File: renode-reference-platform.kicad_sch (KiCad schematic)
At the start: 28 parts

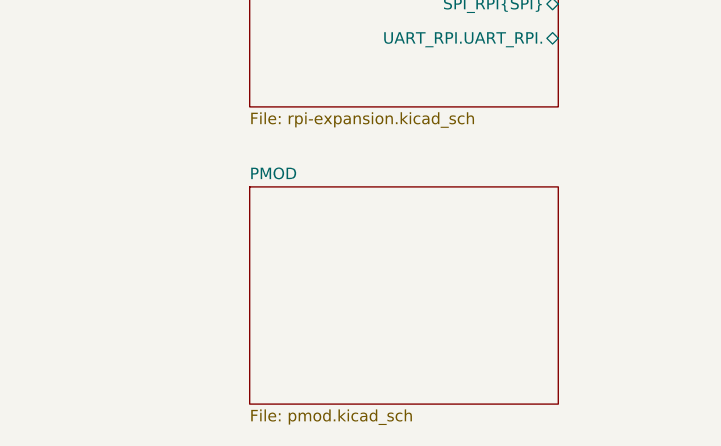
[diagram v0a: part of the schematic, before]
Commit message: [#94862] Add PMOD interfaces
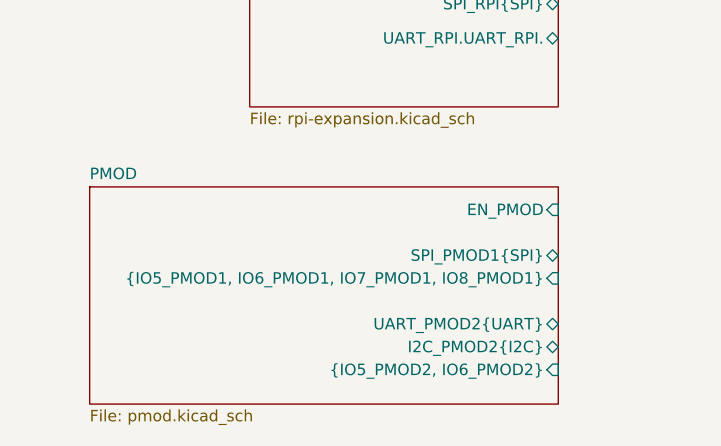
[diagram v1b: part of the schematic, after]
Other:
- sheet PMOD ports: added EN_PMOD, I2C_PMOD2{I2C}, SPI_PMOD1{SPI}, UART_PMOD2{UART}, {IO5_PMOD1, IO6_PMOD1, IO7_PMOD1, IO8_PMOD1}, {IO5_PMOD2, IO6_PMOD2}; removed none
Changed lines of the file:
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@@
 	)
 	(sheet
-		(at 64.77 217.17)
-		(size 34.29 24.13)
+		(at 46.99 217.17)
+		(size 52.07 24.13)
 		(exclude_from_sim no)
 		(in_bom yes)
@@
 		)
 		(property "Sheetname" "PMOD"
-			(at 64.77 216.4584 0)
+			(at 46.99 216.4584 0)
 			(effects
 				(font
@@
 		)
 		(property "Sheetfile" "pmod.kicad_sch"
-			(at 64.77 241.8846 0)
+			(at 46.99 241.8846 0)
 			(effects
 				(font
@@
 			)
 		)
+		(pin "EN_PMOD" input
+			(at 99.06 219.71 0)
+			(effects
+				(font
+					(size 1.27 1.27)
+				)
+				(justify right)
+			)
+		)
+		(pin "I2C_PMOD2{I2C}" bidirectional
+			(at 99.06 234.95 0)
+			(effects
+				(font
+					(size 1.27 1.27)
+				)
+				(justify right)
+			)
+		)
+		(pin "SPI_PMOD1{SPI}" bidirectional
+			(at 99.06 224.79 0)
+			(effects
+				(font
+					(size 1.27 1.27)
+				)
+				(justify right)
+			)
+		)
+		(pin "UART_PMOD2{UART}" bidirectional
+			(at 99.06 232.41 0)
+			(effects
+				(font
+					(size 1.27 1.27)
+				)
+				(justify right)
+			)
+		)
+		(pin "{IO5_PMOD1, IO6_PMOD1, IO7_PMOD1, IO8_PMOD1}" input
+			(at 99.06 227.33 0)
+			(effects
+				(font
+					(size 1.27 1.27)
+				)
+				(justify right)
+			)
+		)
+		(pin "{IO5_PMOD2, IO6_PMOD2}" input
+			(at 99.06 237.49 0)
+			(effects
+				(font
+					(size 1.27 1.27)
+				)
+				(justify right)
+			)
+		)

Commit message: [#94911] Add USB DRP
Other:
- sheet USB-C ports: added I2C_USB{I2C}, USB_GPIO_OUT1, USB_GPIO_OUT2, USB_GPIO_~{INT}; removed none
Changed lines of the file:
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@@
 		)
 		(pin "USB{USB}" bidirectional
+			(at 99.06 123.19 0)
+			(effects
+				(font
+					(size 1.27 1.27)
+				)
+				(justify right)
+			)
+		)
+		(pin "I2C_USB{I2C}" bidirectional
+			(at 99.06 125.73 0)
+			(effects
+				(font
+					(size 1.27 1.27)
+				)
+				(justify right)
+			)
+		)
+		(pin "USB_GPIO_OUT1" input
 			(at 99.06 132.08 0)
 			(effects
 				(font
+					(size 1.27 1.27)
+				)
+				(justify right)
+			)
+		)
+		(pin "USB_GPIO_OUT2" input
+			(at 99.06 134.62 0)
+			(effects
+				(font
+					(size 1.27 1.27)
+				)
+				(justify right)
+			)
+		)
+		(pin "USB_GPIO_~{INT}" input
+			(at 99.06 129.54 0)
+			(effects
+				(font

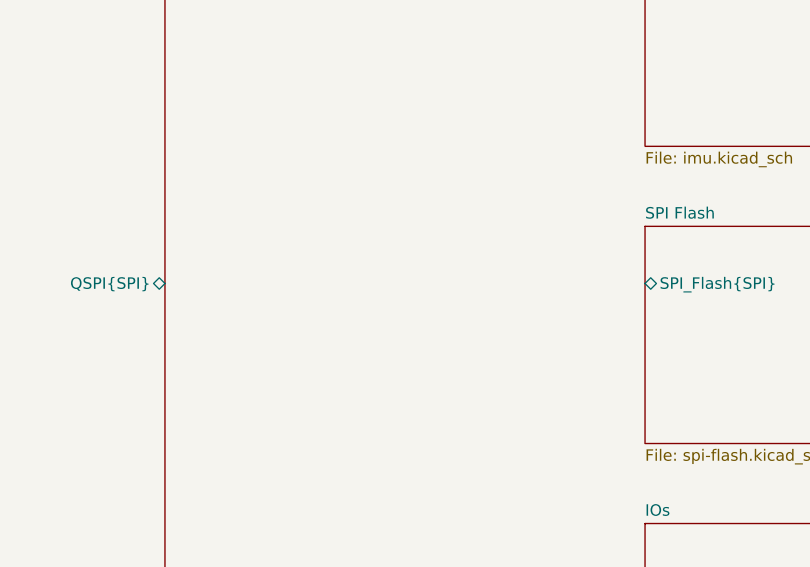
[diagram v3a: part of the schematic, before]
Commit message: [#94972] Reconnect QSPI to MCU
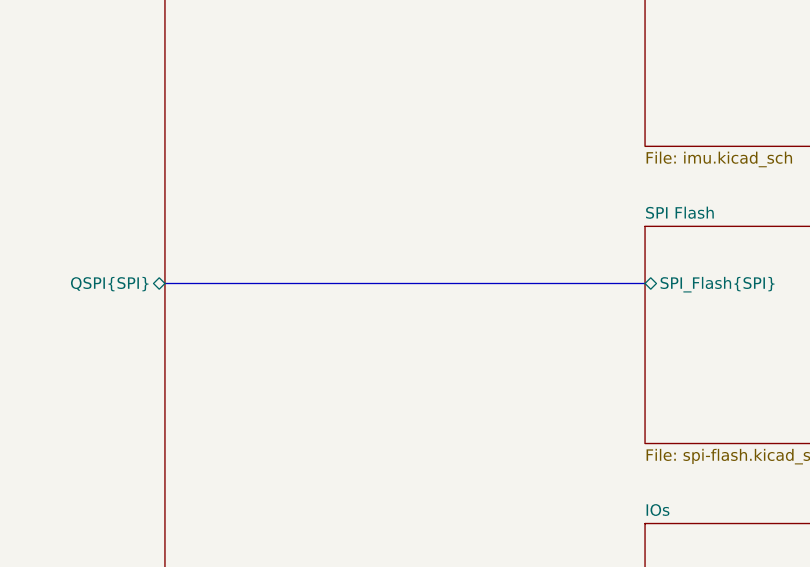
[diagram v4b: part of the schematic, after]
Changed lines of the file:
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@@
+		)
+	)
+	(bus
+		(pts
+			(xy 198.12 157.48) (xy 251.46 157.48)
+		)
+		(stroke
+			(width 0)
+			(type default)
 		)
 	)

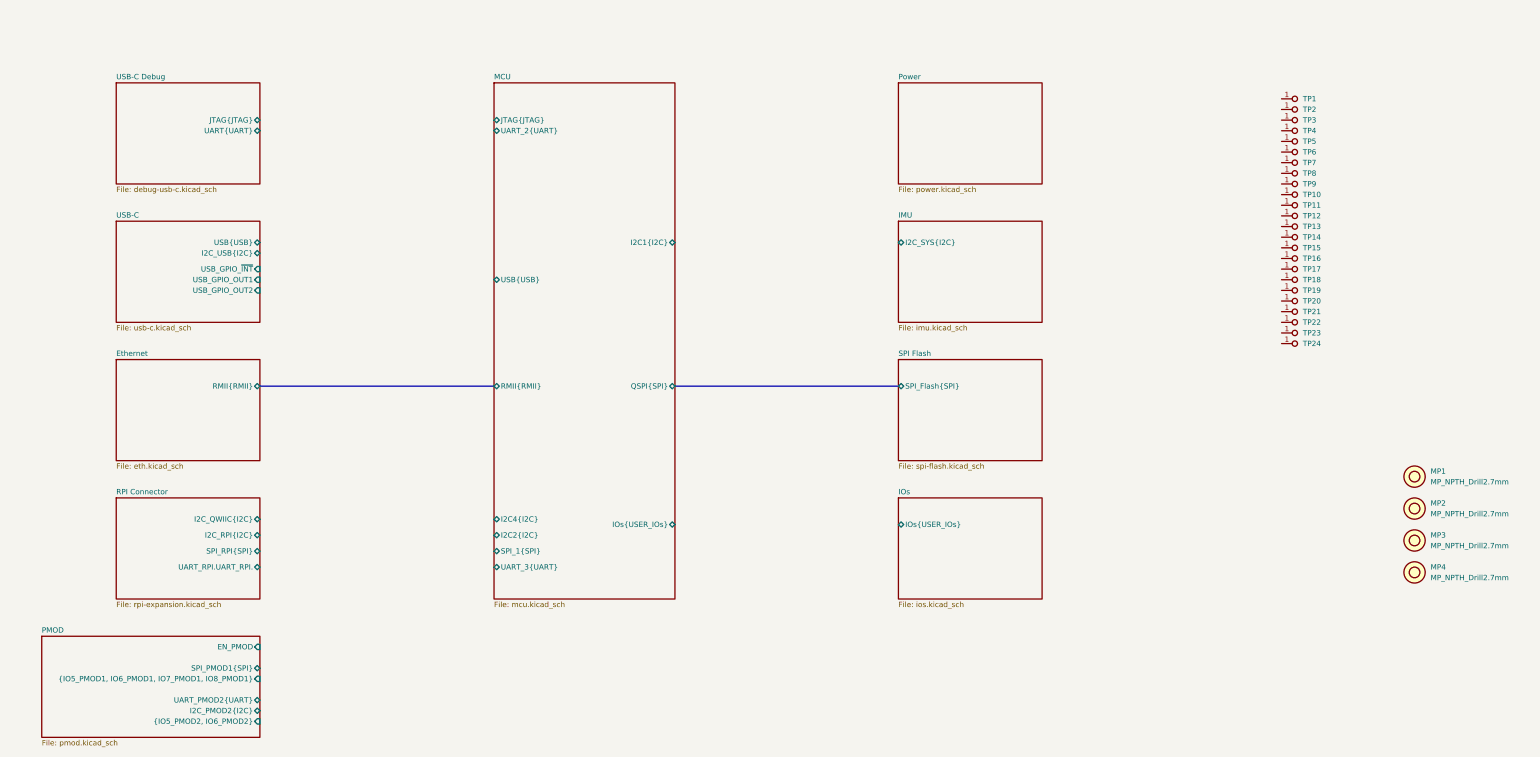
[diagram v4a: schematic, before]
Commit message: [#95036] Rename PMOD signals
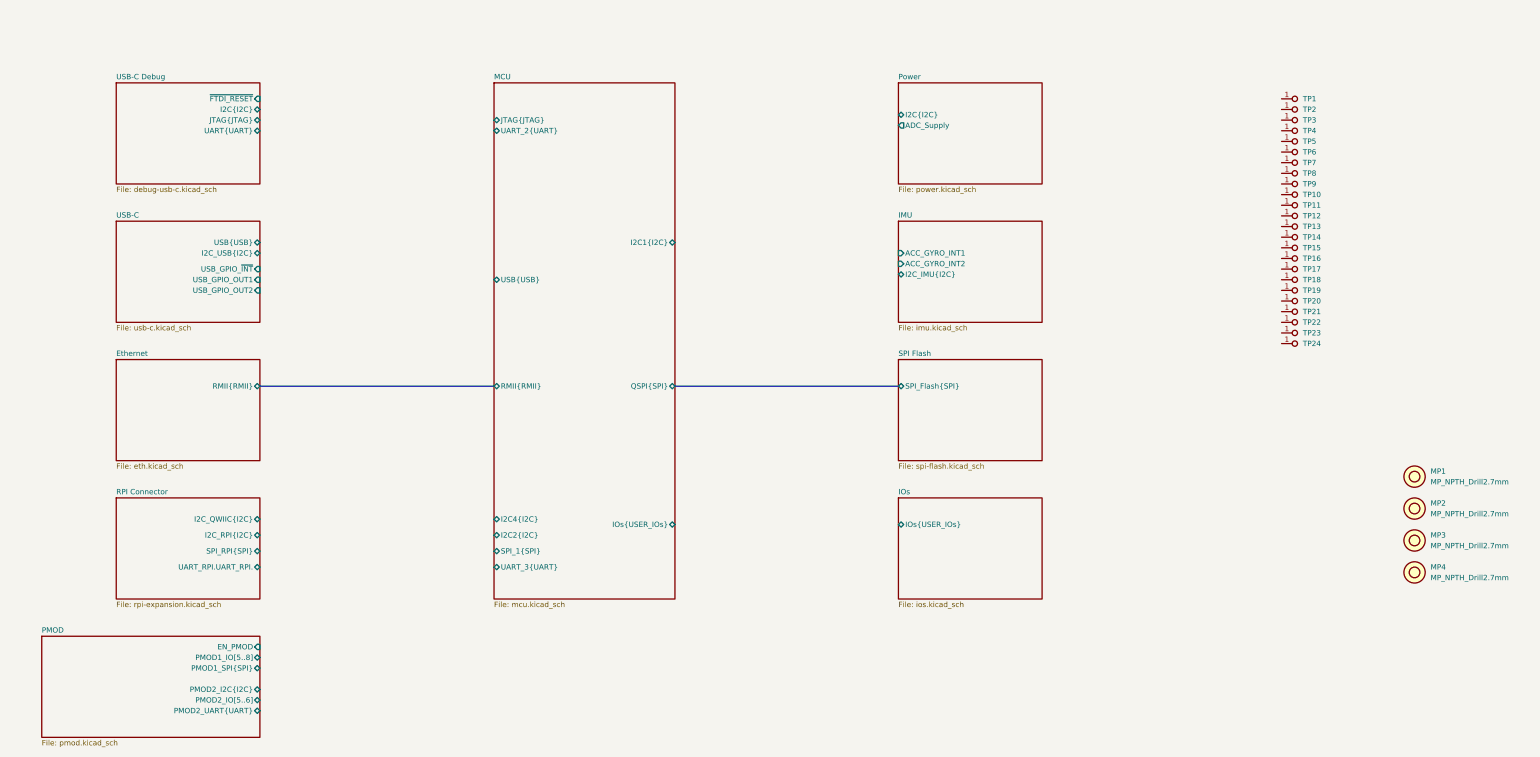
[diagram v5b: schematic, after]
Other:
- sheet IMU ports: added ACC_GYRO_INT1, ACC_GYRO_INT2, I2C_IMU{I2C}; removed I2C_SYS{I2C}
- sheet PMOD ports: added PMOD1_IO[5..8], PMOD1_SPI{SPI}, PMOD2_I2C{I2C}, PMOD2_IO[5..6], PMOD2_UART{UART}; removed I2C_PMOD2{I2C}, SPI_PMOD1{SPI}, UART_PMOD2{UART}, {IO5_PMOD1, IO6_PMOD1, IO7_PMOD1, IO8_PMOD1}, {IO5_PMOD2, IO6_PMOD2}
- sheet Power ports: added ADC_Supply, I2C{I2C}; removed none
- sheet USB-C Debug ports: added I2C{I2C}, ~{FTDI_RESET}; removed none
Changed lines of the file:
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@@
 			)
 		)
-		(pin "I2C_SYS{I2C}" bidirectional
-			(at 251.46 123.19 180)
+		(pin "ACC_GYRO_INT1" input
+			(at 251.46 125.73 180)
+			(effects
+				(font
+					(size 1.27 1.27)
+				)
+				(justify left)
+			)
+		)
+		(pin "ACC_GYRO_INT2" input
+			(at 251.46 128.27 180)
+			(effects
+				(font
+					(size 1.27 1.27)
+				)
+				(justify left)
+			)
+		)
+		(pin "I2C_IMU{I2C}" bidirectional
+			(at 251.46 130.81 180)
 			(effects
 				(font
@@
 			)
 		)
+		(pin "ADC_Supply" output
+			(at 251.46 95.25 180)
+			(effects
+				(font
+					(size 1.27 1.27)
+				)
+				(justify left)
+			)
+		)
+		(pin "I2C{I2C}" bidirectional
+			(at 251.46 92.71 180)
+			(effects
+				(font
+					(size 1.27 1.27)
+				)
+				(justify left)
+			)
+		)
 		(instances
 			(project "renode-reference-platform"
@@
 			)
 		)
-		(pin "I2C_PMOD2{I2C}" bidirectional
+		(pin "PMOD1_IO[5..8]" bidirectional
+			(at 99.06 222.25 0)
+			(effects
+				(font
+					(size 1.27 1.27)
+				)
+				(justify right)
+			)
+		)
+		(pin "PMOD1_SPI{SPI}" bidirectional
+			(at 99.06 224.79 0)
+			(effects
+				(font
+					(size 1.27 1.27)
+				)
+				(justify right)
+			)
+		)
+		(pin "PMOD2_I2C{I2C}" bidirectional
+			(at 99.06 229.87 0)
+			(effects
+				(font
+					(size 1.27 1.27)
+				)
+				(justify right)
+			)
+		)
+		(pin "PMOD2_IO[5..6]" bidirectional
+			(at 99.06 232.41 0)
+			(effects
+				(font
+					(size 1.27 1.27)
+				)
+				(justify right)
+			)
+		)
+		(pin "PMOD2_UART{UART}" bidirectional
 			(at 99.06 234.95 0)
-			(effects
-				(font
-					(size 1.27 1.27)
-				)
-				(justify right)
-			)
-		)
-		(pin "SPI_PMOD1{SPI}" bidirectional
-			(at 99.06 224.79 0)
-			(effects
-				(font
-					(size 1.27 1.27)
-				)
-				(justify right)
-			)
-		)
-		(pin "UART_PMOD2{UART}" bidirectional
-			(at 99.06 232.41 0)
-			(effects
-				(font
-					(size 1.27 1.27)
-				)
-				(justify right)
-			)
-		)
-		(pin "{IO5_PMOD1, IO6_PMOD1, IO7_PMOD1, IO8_PMOD1}" input
-			(at 99.06 227.33 0)
-			(effects
-				(font
-					(size 1.27 1.27)
-				)
-				(justify right)
-			)
-		)
-		(pin "{IO5_PMOD2, IO6_PMOD2}" input
-			(at 99.06 237.49 0)
 			(effects
 				(font
@@
 			(effects
 				(font
+					(size 1.27 1.27)
+				)
+				(justify right)
+			)
+		)
+		(pin "I2C{I2C}" bidirectional
+			(at 99.06 91.44 0)
+			(effects
+				(font
+					(size 1.27 1.27)
+				)
+				(justify right)
+			)
+		)
+		(pin "~{FTDI_RESET}" input
+			(at 99.06 88.9 0)
+			(effects
+				(font

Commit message: [#95036] Reconnect power flags, add GPIOs to RPI connector
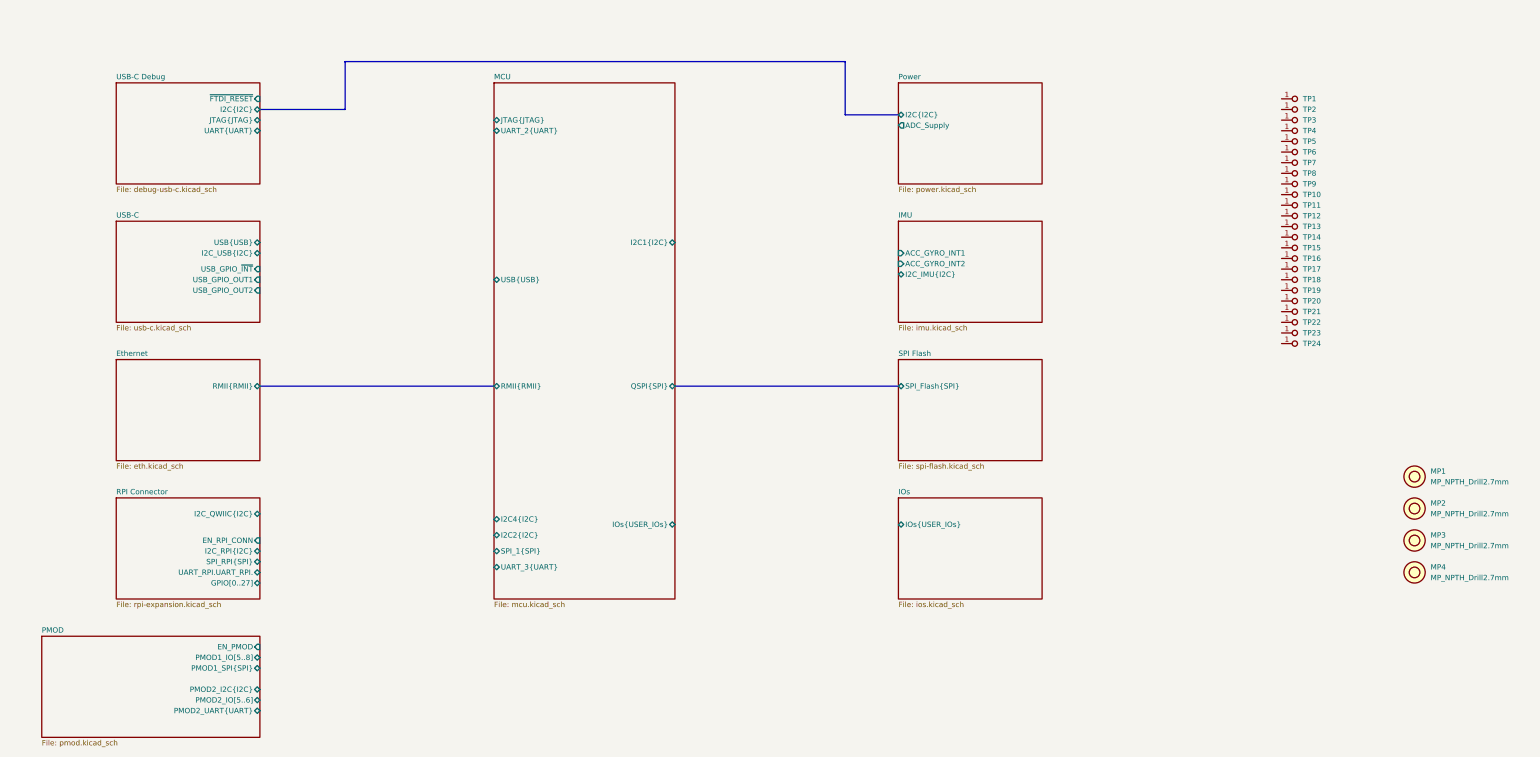
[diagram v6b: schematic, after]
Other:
- sheet RPI Connector ports: added EN_RPI_CONN, GPIO[0..27]; removed none
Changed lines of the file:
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@@
 	(bus
 		(pts
+			(xy 119.38 91.44) (xy 119.38 80.01)
+		)
+		(stroke
+			(width 0)
+			(type default)
+		)
+	)
+	(bus
+		(pts
+			(xy 99.06 91.44) (xy 119.38 91.44)
+		)
+		(stroke
+			(width 0)
+			(type default)
+		)
+	)
+	(bus
+		(pts
 			(xy 99.06 157.48) (xy 154.94 157.48)
 		)
@@
 	(bus
 		(pts
+			(xy 238.76 92.71) (xy 251.46 92.71)
+		)
+		(stroke
+			(width 0)
+			(type default)
+		)
+	)
+	(bus
+		(pts
+			(xy 119.38 80.01) (xy 238.76 80.01)
+		)
+		(stroke
+			(width 0)
+			(type default)
+		)
+	)
+	(bus
+		(pts
 			(xy 198.12 157.48) (xy 251.46 157.48)
 		)
@@
 		)
 	)
+	(bus
+		(pts
+			(xy 238.76 80.01) (xy 238.76 92.71)
+		)
+		(stroke
+			(width 0)
+			(type default)
+		)
+	)
 	(image
 		(at -38.1 110.49)
@@
 		)
 		(pin "I2C_QWIIC{I2C}" bidirectional
-			(at 99.06 189.23 0)
+			(at 99.06 187.96 0)
 			(effects
 				(font
@@
 		)
 		(pin "I2C_RPI{I2C}" bidirectional
-			(at 99.06 193.04 0)
+			(at 99.06 196.85 0)
 			(effects
 				(font
@@
 		)
 		(pin "SPI_RPI{SPI}" bidirectional
-			(at 99.06 196.85 0)
+			(at 99.06 199.39 0)
 			(effects
 				(font
@@
 		)
 		(pin "UART_RPI.UART_RPI." bidirectional
-			(at 99.06 200.66 0)
+			(at 99.06 201.93 0)
+			(effects
+				(font
+					(size 1.27 1.27)
+				)
+				(justify right)
+			)
+		)
+		(pin "EN_RPI_CONN" input
+			(at 99.06 194.31 0)
+			(effects
+				(font
+					(size 1.27 1.27)
+				)
+				(justify right)
+			)
+		)
+		(pin "GPIO[0..27]" bidirectional
+			(at 99.06 204.47 0)
 			(effects
 				(font
